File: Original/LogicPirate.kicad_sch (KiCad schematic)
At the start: 19 parts

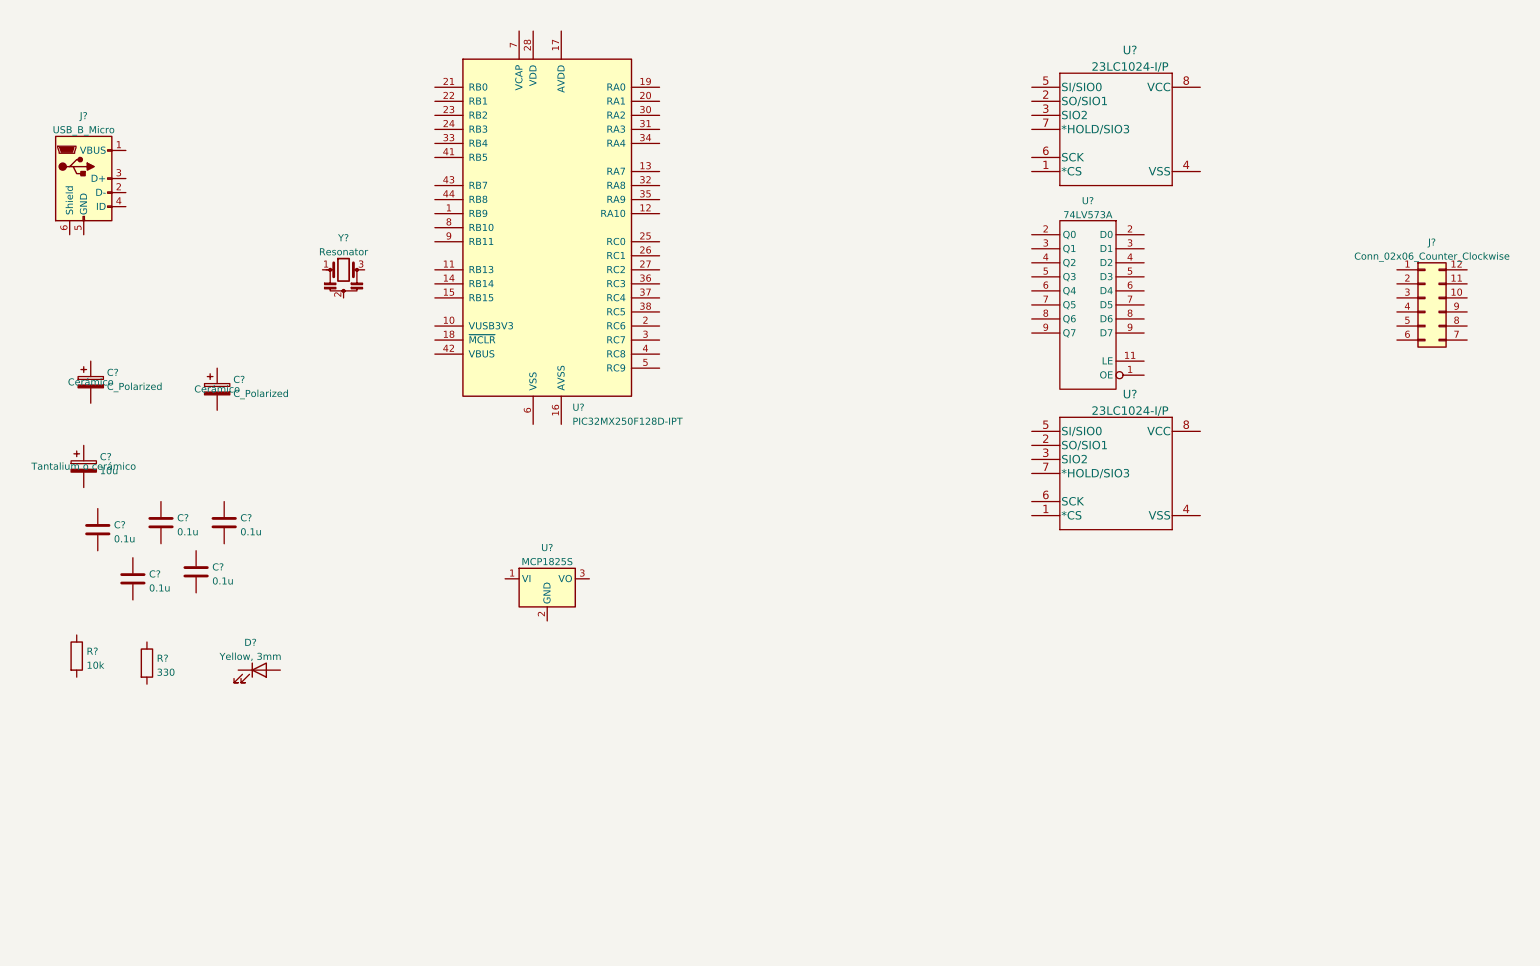
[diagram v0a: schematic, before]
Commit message: SCH. Completo, primera revision
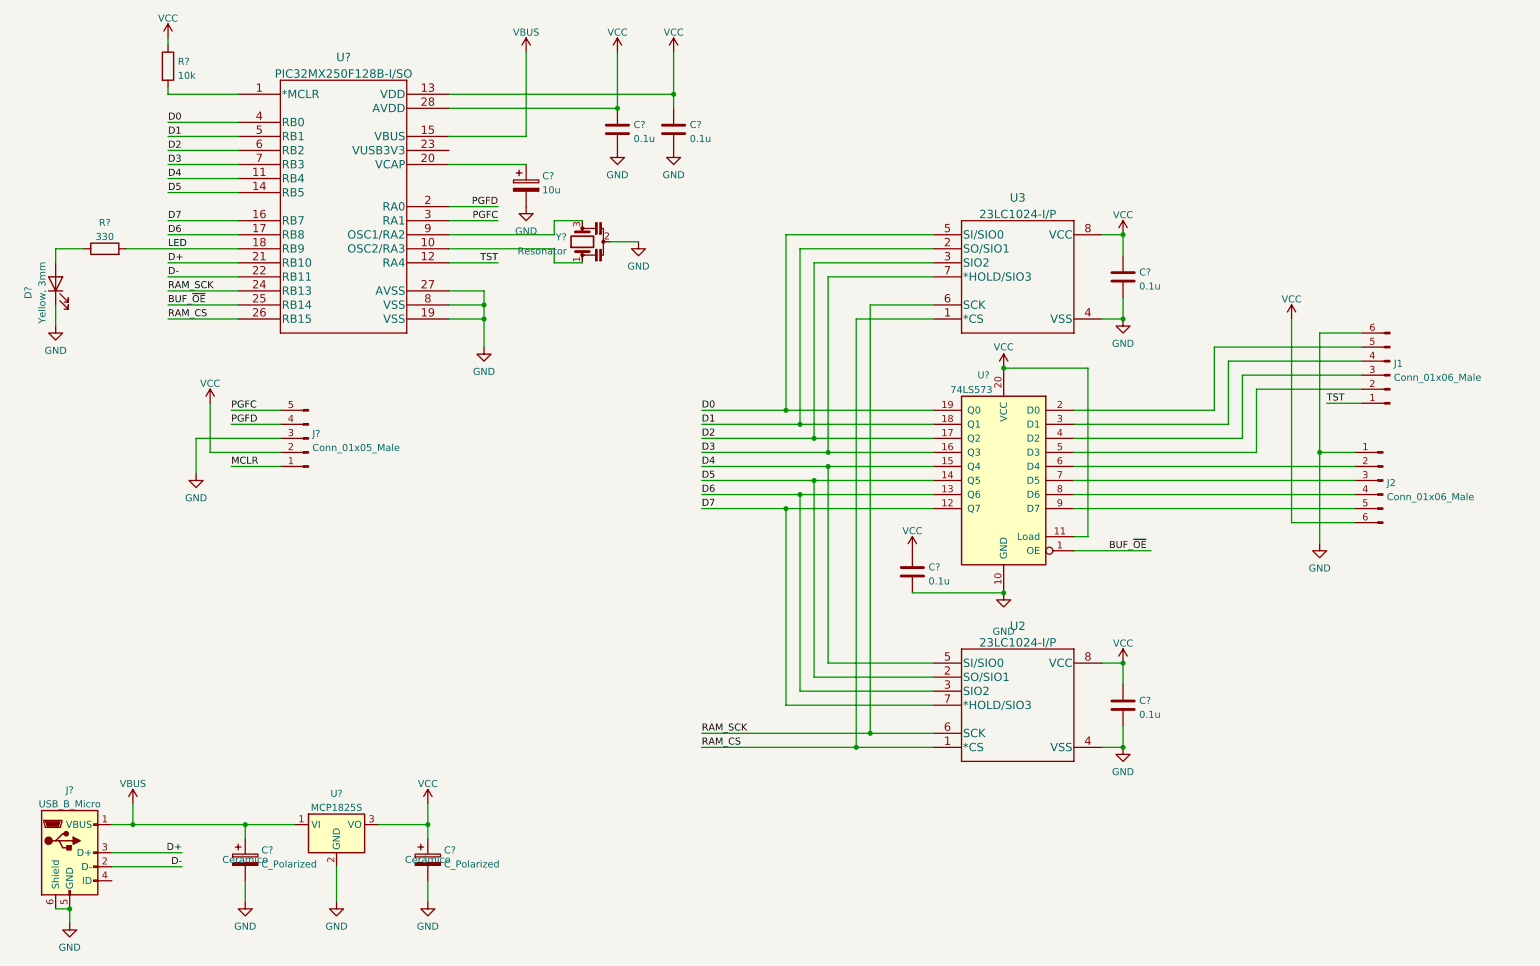
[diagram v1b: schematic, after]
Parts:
- removed J?: Conn_02x06_Counter_Clockwise, Connector_PinHeader_2.54mm:PinHeader_2x06_P2.54mm_Vertical, symbol Connector_Generic:Conn_02x06_Counter_Clockwise
- removed U?: 74LV573A, symbol Tochi:74LV573A
- removed U?: PIC32MX250F128D-IPT, Package_QFP_AKL:TQFP-44_10x10mm_P0.8mm, symbol MCU_Microchip_PIC32:PIC32MX250F128D-IPT
- added J1, J2: Conn_01x06_Male, symbol Connector:Conn_01x06_Male
- added J?: Conn_01x05_Male, symbol Connector:Conn_01x05_Male
- added U?: PIC32MX250F128B-I/SO, SOIC28-W_MC_MCH, symbol PIC32MX250F128B-I-SO:PIC32MX250F128B-I/SO
- added U?: 74LS573, symbol 74xx:74LS573
- gave numbers to parts that had none: 2
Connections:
- net at R?.1: now also D?.2 (A)
- net LED: now reaches R?.2
- net LED: now also U?.18 (RB9)
- net VCC: now reaches C?.1
- net VCC: now also C?.1, C?.1, C?.1, C?.1, C?.1, R?.1, U2.8 (VCC), U3.8 (VCC), U?.3 (VO), J2.6 (Pin_6), J?.2 (Pin_2), U?.11 (Load), U?.13 (VDD), U?.20 (VCC), U?.28 (AVDD)
- net GND: now reaches C?.2
- net GND: now also C?.2, C?.2, C?.2, C?.2, C?.2, C?.2, C?.2, D?.1 (K), J?.5 (GND), J?.6 (Shield), U2.4 (VSS), U3.4 (VSS), U?.2 (GND), Y?.2, J1.6 (Pin_6), J2.1 (Pin_1), J?.3 (Pin_3), U?.10 (GND), U?.19 (VSS), U?.27 (AVSS), U?.8 (VSS)
- net RAM_CS: now reaches U2.1 (*CS)
- net RAM_CS: now also U3.1 (*CS), U?.26 (RB15)
- net D5: now reaches U2.2 (SO/SIO1)
- net D5: now also U?.14 (Q5), U?.14 (RB5)
- net D6: now reaches U2.3 (SIO2)
- net D6: now also U?.13 (Q6), U?.17 (RB8)
- net D4: now reaches U2.5 (SI/SIO0)
- net D4: now also U?.11 (RB4), U?.15 (Q4)
- net RAM_SCK: now reaches U2.6 (SCK)
- net RAM_SCK: now also U3.6 (SCK), U?.24 (RB13)
- net D7: now reaches U2.7 (*HOLD/SIO3)
- net D7: now also U?.12 (Q7), U?.16 (RB7)
- net VBUS: now reaches C?.1
- net VBUS: now also J?.1 (VBUS), U?.1 (VI), U?.15 (VBUS)
- net at R?.2: now also U?.1 (*MCLR)
- net D1: now reaches U3.2 (SO/SIO1)
- net D1: now also U?.18 (Q1), U?.5 (RB1)
- net D2: now reaches U3.3 (SIO2)
- net D2: now also U?.17 (Q2), U?.6 (RB2)
- net D0: now reaches U3.5 (SI/SIO0)
- net D0: now also U?.19 (Q0), U?.4 (RB0)
- net D3: now reaches U3.7 (*HOLD/SIO3)
- net D3: now also U?.16 (Q3), U?.7 (RB3)
- net D-: now reaches J?.2 (D-)
- net D-: now also U?.22 (RB11)
- net D+: now reaches J?.3 (D+)
- net D+: now also U?.21 (RB10)
- net at C?.1: now also U?.20 (VCAP)
- net at Y?.1: now also U?.10 (OSC2/RA3)
- net at Y?.3: now also U?.9 (OSC1/RA2)
- new net: J1.2 (Pin_2), U?.5 (D3)
- new net: J1.3 (Pin_3), U?.4 (D2)
- new net: J1.4 (Pin_4), U?.3 (D1)
- new net: J1.5 (Pin_5), U?.2 (D0)
- new net: J2.2 (Pin_2), U?.6 (D4)
- new net: J2.3 (Pin_3), U?.7 (D5)
- new net: J2.4 (Pin_4), U?.8 (D6)
- new net: J2.5 (Pin_5), U?.9 (D7)
- new net BUF_~{OE}: U?.1 (OE), U?.25 (RB14)
- new net MCLR: J?.1 (Pin_1)
- new net PGFC: J?.5 (Pin_5), U?.3 (RA1)
- new net PGFD: J?.4 (Pin_4), U?.2 (RA0)
- new net TST: J1.1 (Pin_1), U?.12 (RA4)
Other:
- moved on the sheet: C?, D?, J?, R?, U2, U3, U?, Y?

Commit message: small fixes
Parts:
- U?: value 74LS573 -> 74LVC573
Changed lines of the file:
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@@
       (effects (font (size 1.27 1.27)) (justify left))
     )
-    (property "Value" "74LS573" (id 1) (at 192.2906 91.5471 0)
+    (property "Value" "74LVC573" (id 1) (at 192.2906 91.5471 0)
       (effects (font (size 1.27 1.27)) (justify left))
     )
@@
     )
     (path "/b022c481-021a-4875-9105-57eb8351a9db"
-      (reference "U?") (unit 1) (value "74LS573") (footprint "")
+      (reference "U?") (unit 1) (value "74LVC573") (footprint "")
     )
     (path "/c0b00728-8da5-4fbb-bf91-d770374191e9"
